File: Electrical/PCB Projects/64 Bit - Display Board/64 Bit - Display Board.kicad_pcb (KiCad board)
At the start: 4 copper layers, 200 x 75.1 mm, 60 parts, among them J1 Conn_01x03, J2 Conn_01x03, P1 610110249121, P2 610110249121, P3 610110249121, T1 IN-12A, T10 IN-12A, T2 IN-12A, T5 IN-12A, T6 IN-12A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

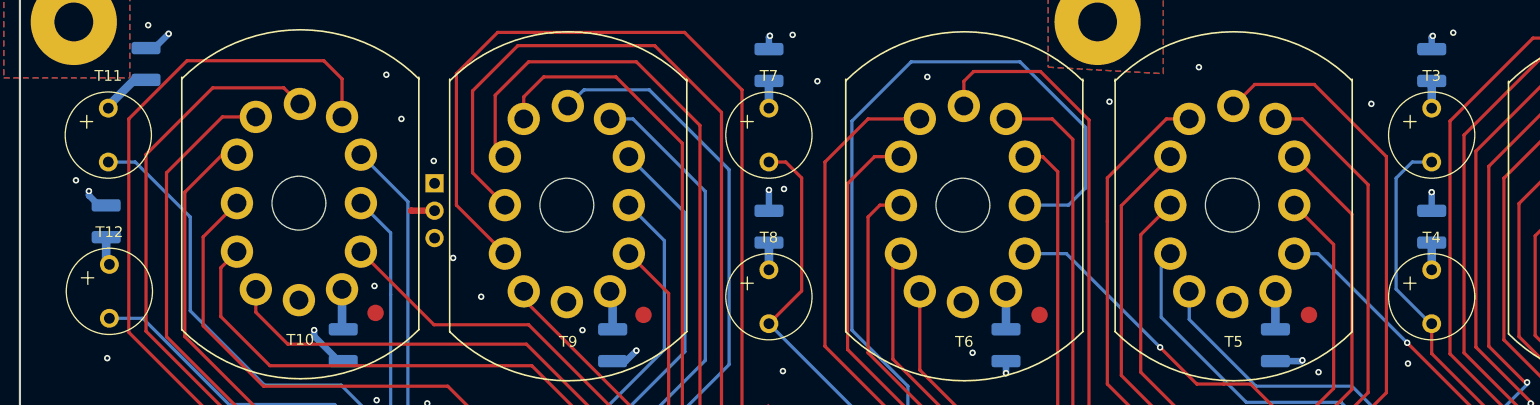
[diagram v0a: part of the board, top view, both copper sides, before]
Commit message: near final state. Includes BOM, price, etc
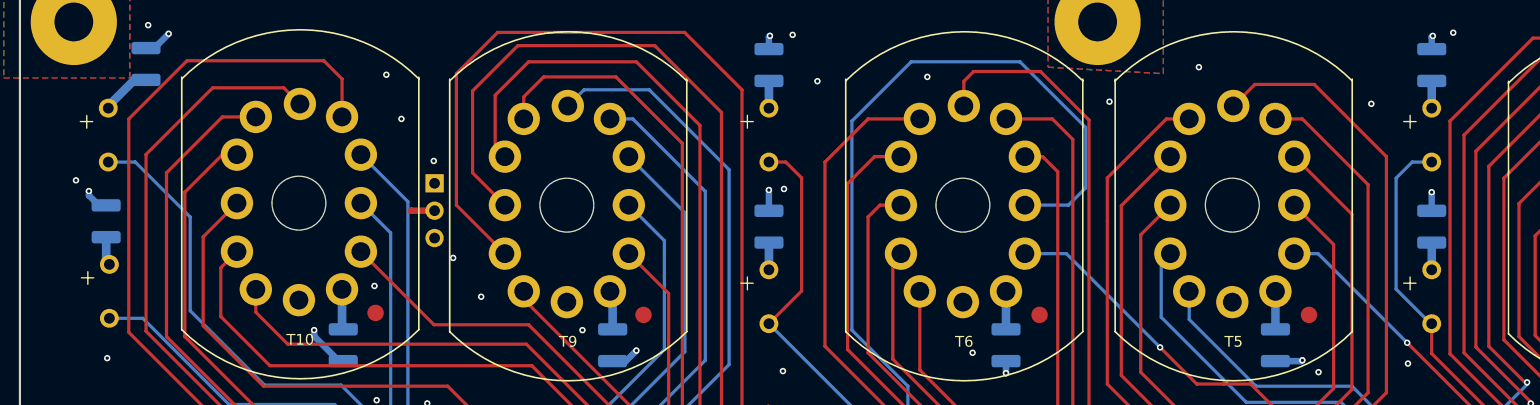
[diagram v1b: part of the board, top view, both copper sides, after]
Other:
- board text added: "'64 Bit' Nixie Tube Clock - Display Board_V1.0 Dec 2025"
- board text removed: "'64 Bit' Nixie Tube Clock - Display Board_V1.0 Oct 2025"
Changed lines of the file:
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@@
 			(drillshape 0)
 			(scaleselection 1)
-			(outputdirectory "G:/My Drive/Projects (GDrive)/31_My First Nixie Clock/01_My First Nixie Clock/PCB Plots/Display Board/Gerber Files/")
+			(outputdirectory "C:/Users/Kadin/Desktop/Git Projects/64-Bit/Electrical/PCB Outputs/64 Bit - Display Board/gerbers/")
 		)
 	)
@@
 			(at 0 -5.5 0)
 			(unlocked yes)
-			(layer "F.SilkS")
+			(layer "F.Fab")
 			(effects
 				(font
@@
 			)
 			(fill no)
-			(layer "F.SilkS")
+			(layer "F.Fab")
 		)
 		(fp_text user "${REFERENCE}"
@@
 			(at 0 -5.5 0)
 			(unlocked yes)
-			(layer "F.SilkS")
+			(layer "F.Fab")
 			(effects
 				(font
@@
 			)
 			(fill no)
-			(layer "F.SilkS")
+			(layer "F.Fab")
 		)
 		(fp_text user "${REFERENCE}"
@@
 			(at 0 -5.5 0)
 			(unlocked yes)
-			(layer "F.SilkS")
+			(layer "F.Fab")
 			(effects
 				(font
@@
 			)
 			(fill no)
-			(layer "F.SilkS")
+			(layer "F.Fab")
 		)
 		(fp_text user "${REFERENCE}"
@@
 			(at 0 -5.5 0)
 			(unlocked yes)
-			(layer "F.SilkS")
+			(layer "F.Fab")
 			(effects
 				(font
@@
 			)
 			(fill no)
-			(layer "F.SilkS")
+			(layer "F.Fab")
 		)
 		(fp_text user "${REFERENCE}"
@@
 			(at 0 -5.5 0)
 			(unlocked yes)
-			(layer "F.SilkS")
+			(layer "F.Fab")
 			(effects
 				(font
@@
 			)
 			(fill no)
-			(layer "F.SilkS")
+			(layer "F.Fab")
 		)
 		(fp_text user "${REFERENCE}"
@@
 			(at 0 -5.5 0)
 			(unlocked yes)
-			(layer "F.SilkS")
+			(layer "F.Fab")
 			(effects
 				(font
@@
 			)
 			(fill no)
-			(layer "F.SilkS")
+			(layer "F.Fab")
 		)
 		(fp_text user "${REFERENCE}"
@@
 		)
 	)
-	(gr_text "'64 Bit' Nixie Tube Clock - Display Board_V1.0 Oct 2025"
+	(gr_text "'64 Bit' Nixie Tube Clock - Display Board_V1.0 Dec 2025"
 		(at 96.9 120.9 0)
 		(layer "F.Mask")
